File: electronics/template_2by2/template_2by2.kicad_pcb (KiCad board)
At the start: 2 copper layers, 19 x 34 mm, 8 parts, among them J1 1, J2 2, J3 3, J4 4, J5 5, J6 6

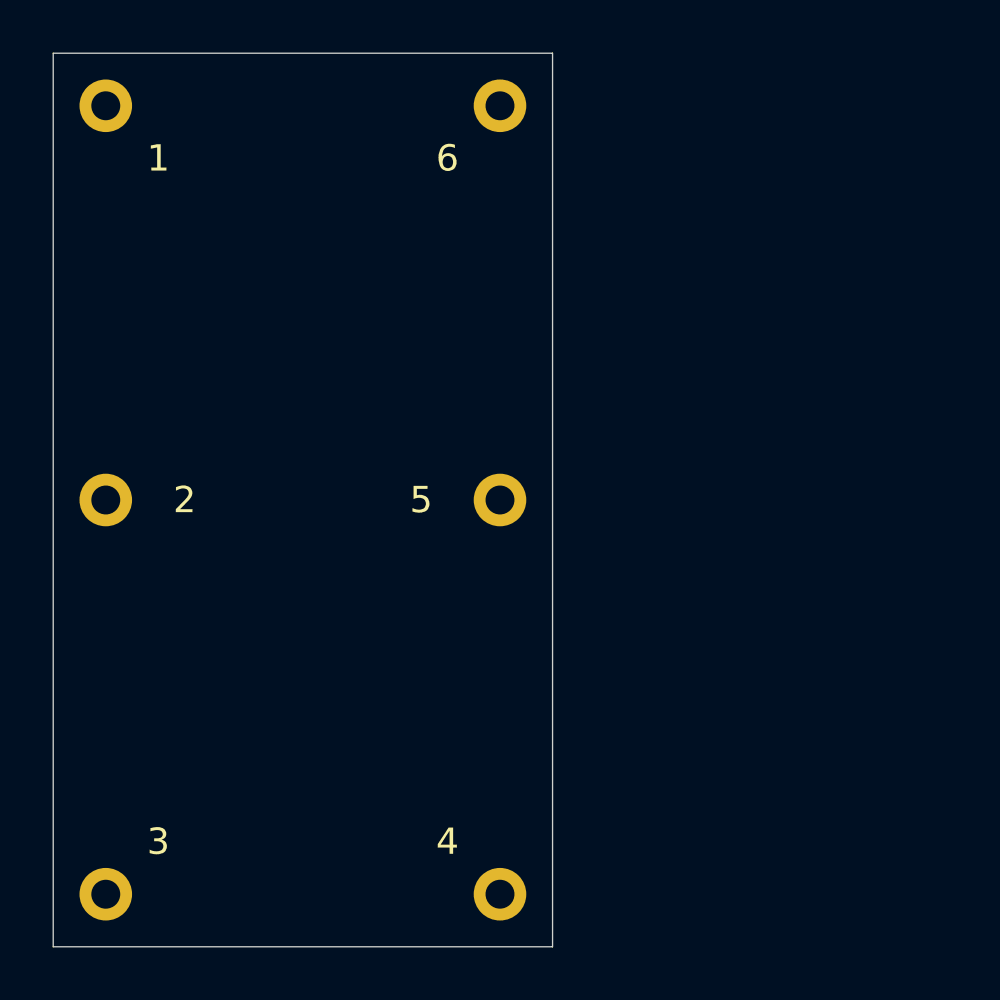
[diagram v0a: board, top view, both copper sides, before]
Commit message: finished 2 by 2 unit template
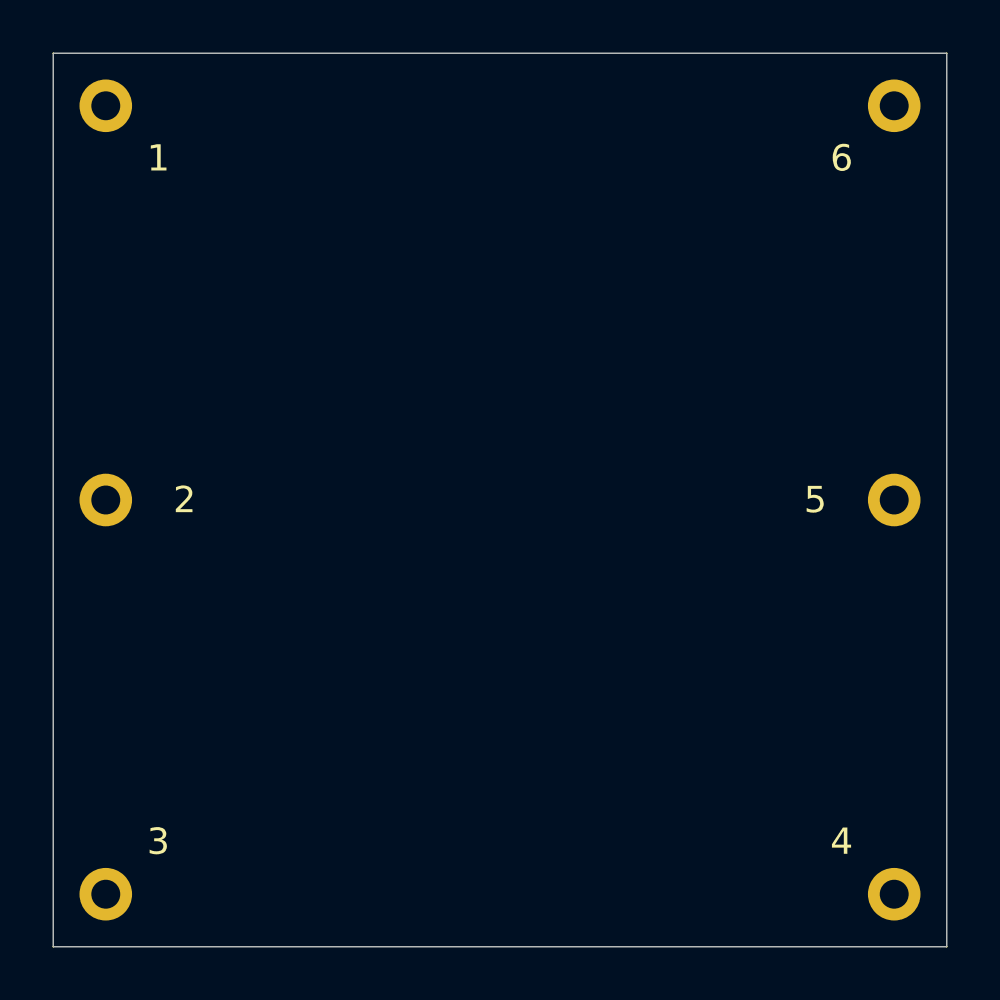
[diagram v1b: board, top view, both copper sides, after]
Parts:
- moved J4 15.0 mm to (172.0, 93.0)
- moved J5 15.0 mm to (172.0, 78.0)
- moved J6 15.0 mm to (172.0, 63.0)
- moved N1 7.00 mm to (156.0, 82.0)
- moved N2 7.00 mm to (157.0, 78.0)
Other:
- board size 19 x 34 mm -> 34 x 34 mm
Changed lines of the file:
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@@
     (add_net "Net-(J1-Pad1)")
   )
-  (module mill-max:PC_pin_nail_head_6092 (layer F.Cu)
-    (at 157 63)
+  (module mill-max:PC_pin_nail_head_6092 locked (layer F.Cu)
+    (at 172 63)
     (fp_text reference J6 (at -2 2) (layer F.Fab)
       (effects (font (size 1 1) (thickness 0.15)))
@@
       (effects (font (size 1 1) (thickness 0.15)))
     )
+    (fp_circle (center 0 0) (end 1.3 0) (layer B.CrtYd) (width 0.025))
     (fp_circle (center 0 0) (end 1.3 0) (layer F.CrtYd) (width 0.025))
-    (fp_circle (center 0 0) (end 1.3 0) (layer B.CrtYd) (width 0.025))
     (pad 1 thru_hole circle (at 0 0) (size 2 2) (drill 1.1) (layers *.Cu *.Mask)
       (net 1 "Net-(J1-Pad1)"))
   )
-  (module mill-max:PC_pin_nail_head_6092 (layer F.Cu)
-    (at 157 78)
+  (module mill-max:PC_pin_nail_head_6092 locked (layer F.Cu)
+    (at 172 78)
     (fp_text reference J5 (at -3 0) (layer F.Fab)
       (effects (font (size 1 1) (thickness 0.15)))
@@
       (effects (font (size 1 1) (thickness 0.15)))
     )
+    (fp_circle (center 0 0) (end 1.3 0) (layer B.CrtYd) (width 0.025))
     (fp_circle (center 0 0) (end 1.3 0) (layer F.CrtYd) (width 0.025))
-    (fp_circle (center 0 0) (end 1.3 0) (layer B.CrtYd) (width 0.025))
     (pad 1 thru_hole circle (at 0 0) (size 2 2) (drill 1.1) (layers *.Cu *.Mask)
       (net 1 "Net-(J1-Pad1)"))
   )
   (module mill-max:PC_pin_nail_head_6092 locked (layer F.Cu)
-    (at 157 93)
+    (at 172 93)
     (fp_text reference J4 (at -2 -2) (layer F.Fab)
       (effects (font (size 1 1) (thickness 0.15)))
@@
       (effects (font (size 1 1) (thickness 0.15)))
     )
+    (fp_circle (center 0 0) (end 1.3 0) (layer F.CrtYd) (width 0.025))
     (fp_circle (center 0 0) (end 1.3 0) (layer B.CrtYd) (width 0.025))
-    (fp_circle (center 0 0) (end 1.3 0) (layer F.CrtYd) (width 0.025))
     (pad 1 thru_hole circle (at 0 0) (size 2 2) (drill 1.1) (layers *.Cu *.Mask)
       (net 1 "Net-(J1-Pad1)"))
@@
       (effects (font (size 1 1) (thickness 0.15)))
     )
+    (fp_circle (center 0 0) (end 1.3 0) (layer F.CrtYd) (width 0.025))
     (fp_circle (center 0 0) (end 1.3 0) (layer B.CrtYd) (width 0.025))
-    (fp_circle (center 0 0) (end 1.3 0) (layer F.CrtYd) (width 0.025))
     (pad 1 thru_hole circle (at 0 0) (size 2 2) (drill 1.1) (layers *.Cu *.Mask)
       (net 1 "Net-(J1-Pad1)"))
@@
       (effects (font (size 1 1) (thickness 0.15)))
     )
+    (fp_circle (center 0 0) (end 1.3 0) (layer F.CrtYd) (width 0.025))
     (fp_circle (center 0 0) (end 1.3 0) (layer B.CrtYd) (width 0.025))
-    (fp_circle (center 0 0) (end 1.3 0) (layer F.CrtYd) (width 0.025))
     (pad 1 thru_hole circle (at 0 0) (size 2 2) (drill 1.1) (layers *.Cu *.Mask)
       (net 1 "Net-(J1-Pad1)"))
@@
       (effects (font (size 1 1) (thickness 0.15)))
     )
+    (fp_circle (center 0 0) (end 1.3 0) (layer F.CrtYd) (width 0.025))
     (fp_circle (center 0 0) (end 1.3 0) (layer B.CrtYd) (width 0.025))
-    (fp_circle (center 0 0) (end 1.3 0) (layer F.CrtYd) (width 0.025))
     (pad 1 thru_hole circle (at 0 0) (size 2 2) (drill 1.1) (layers *.Cu *.Mask)
       (net 1 "Net-(J1-Pad1)"))
   )
   (module Symbol:OSHW-Symbol_6.7x6mm_SilkScreen (layer B.Cu)
-    (at 150 78 180)
+    (at 157 78 180)
     (descr "Open Source Hardware Symbol")
     (tags "Logo Symbol OSHW")
@@
   )
   (module SquantorLabels:Label_Generic (layer B.Cu)
-    (at 149 82)
+    (at 156 82)
     (descr "Label for general purpose use")
     (tags Label)
@@
     (fp_line (start -0.5 -0.6) (end 0.5 -0.6) (layer B.SilkS) (width 0.15))
   )
-  (gr_line (start 159 61) (end 140 61) (layer Edge.Cuts) (width 0.05))
-  (gr_line (start 159 61) (end 159 95) (layer Edge.Cuts) (width 0.05))
-  (gr_line (start 140 95) (end 159 95) (layer Edge.Cuts) (width 0.05))
+  (gr_line (start 174 61) (end 140 61) (layer Edge.Cuts) (width 0.05))
+  (gr_line (start 174 61) (end 174 95) (layer Edge.Cuts) (width 0.05))
+  (gr_line (start 140 95) (end 174 95) (layer Edge.Cuts) (width 0.05))
   (gr_line (start 140 95) (end 140 61) (layer Edge.Cuts) (width 0.05))
 )

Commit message: locked pins and updated versionnumber
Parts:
- N1: value 20201119 -> 20201120
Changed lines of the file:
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@@
       (effects (font (size 1 1) (thickness 0.15)))
     )
+    (fp_circle (center 0 0) (end 1.3 0) (layer F.CrtYd) (width 0.025))
     (fp_circle (center 0 0) (end 1.3 0) (layer B.CrtYd) (width 0.025))
-    (fp_circle (center 0 0) (end 1.3 0) (layer F.CrtYd) (width 0.025))
     (pad 1 thru_hole circle (at 0 0) (size 2 2) (drill 1.1) (layers *.Cu *.Mask)
       (net 1 "Net-(J1-Pad1)"))
@@
       (effects (font (size 1 1) (thickness 0.15)))
     )
+    (fp_circle (center 0 0) (end 1.3 0) (layer F.CrtYd) (width 0.025))
     (fp_circle (center 0 0) (end 1.3 0) (layer B.CrtYd) (width 0.025))
-    (fp_circle (center 0 0) (end 1.3 0) (layer F.CrtYd) (width 0.025))
     (pad 1 thru_hole circle (at 0 0) (size 2 2) (drill 1.1) (layers *.Cu *.Mask)
       (net 1 "Net-(J1-Pad1)"))
@@
       (effects (font (size 1 1) (thickness 0.15)))
     )
+    (fp_circle (center 0 0) (end 1.3 0) (layer B.CrtYd) (width 0.025))
     (fp_circle (center 0 0) (end 1.3 0) (layer F.CrtYd) (width 0.025))
-    (fp_circle (center 0 0) (end 1.3 0) (layer B.CrtYd) (width 0.025))
     (pad 1 thru_hole circle (at 0 0) (size 2 2) (drill 1.1) (layers *.Cu *.Mask)
       (net 1 "Net-(J1-Pad1)"))
@@
       (effects (font (size 1 1) (thickness 0.15)))
     )
+    (fp_circle (center 0 0) (end 1.3 0) (layer B.CrtYd) (width 0.025))
     (fp_circle (center 0 0) (end 1.3 0) (layer F.CrtYd) (width 0.025))
-    (fp_circle (center 0 0) (end 1.3 0) (layer B.CrtYd) (width 0.025))
     (pad 1 thru_hole circle (at 0 0) (size 2 2) (drill 1.1) (layers *.Cu *.Mask)
       (net 1 "Net-(J1-Pad1)"))
@@
       (effects (font (size 1 1) (thickness 0.15)))
     )
+    (fp_circle (center 0 0) (end 1.3 0) (layer B.CrtYd) (width 0.025))
     (fp_circle (center 0 0) (end 1.3 0) (layer F.CrtYd) (width 0.025))
-    (fp_circle (center 0 0) (end 1.3 0) (layer B.CrtYd) (width 0.025))
     (pad 1 thru_hole circle (at 0 0) (size 2 2) (drill 1.1) (layers *.Cu *.Mask)
       (net 1 "Net-(J1-Pad1)"))
@@
       (effects (font (size 1 1) (thickness 0.15)))
     )
+    (fp_circle (center 0 0) (end 1.3 0) (layer B.CrtYd) (width 0.025))
     (fp_circle (center 0 0) (end 1.3 0) (layer F.CrtYd) (width 0.025))
-    (fp_circle (center 0 0) (end 1.3 0) (layer B.CrtYd) (width 0.025))
     (pad 1 thru_hole circle (at 0 0) (size 2 2) (drill 1.1) (layers *.Cu *.Mask)
       (net 1 "Net-(J1-Pad1)"))
@@
       (effects (font (size 1 1) (thickness 0.15)) (justify mirror))
     )
-    (fp_text value 20201119 (at 0.8 0.1) (layer B.SilkS)
+    (fp_text value 20201120 (at 0.8 0.1) (layer B.SilkS)
       (effects (font (size 0.8 0.8) (thickness 0.15)) (justify mirror))
     )
